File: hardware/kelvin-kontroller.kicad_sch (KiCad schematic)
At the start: 22 parts

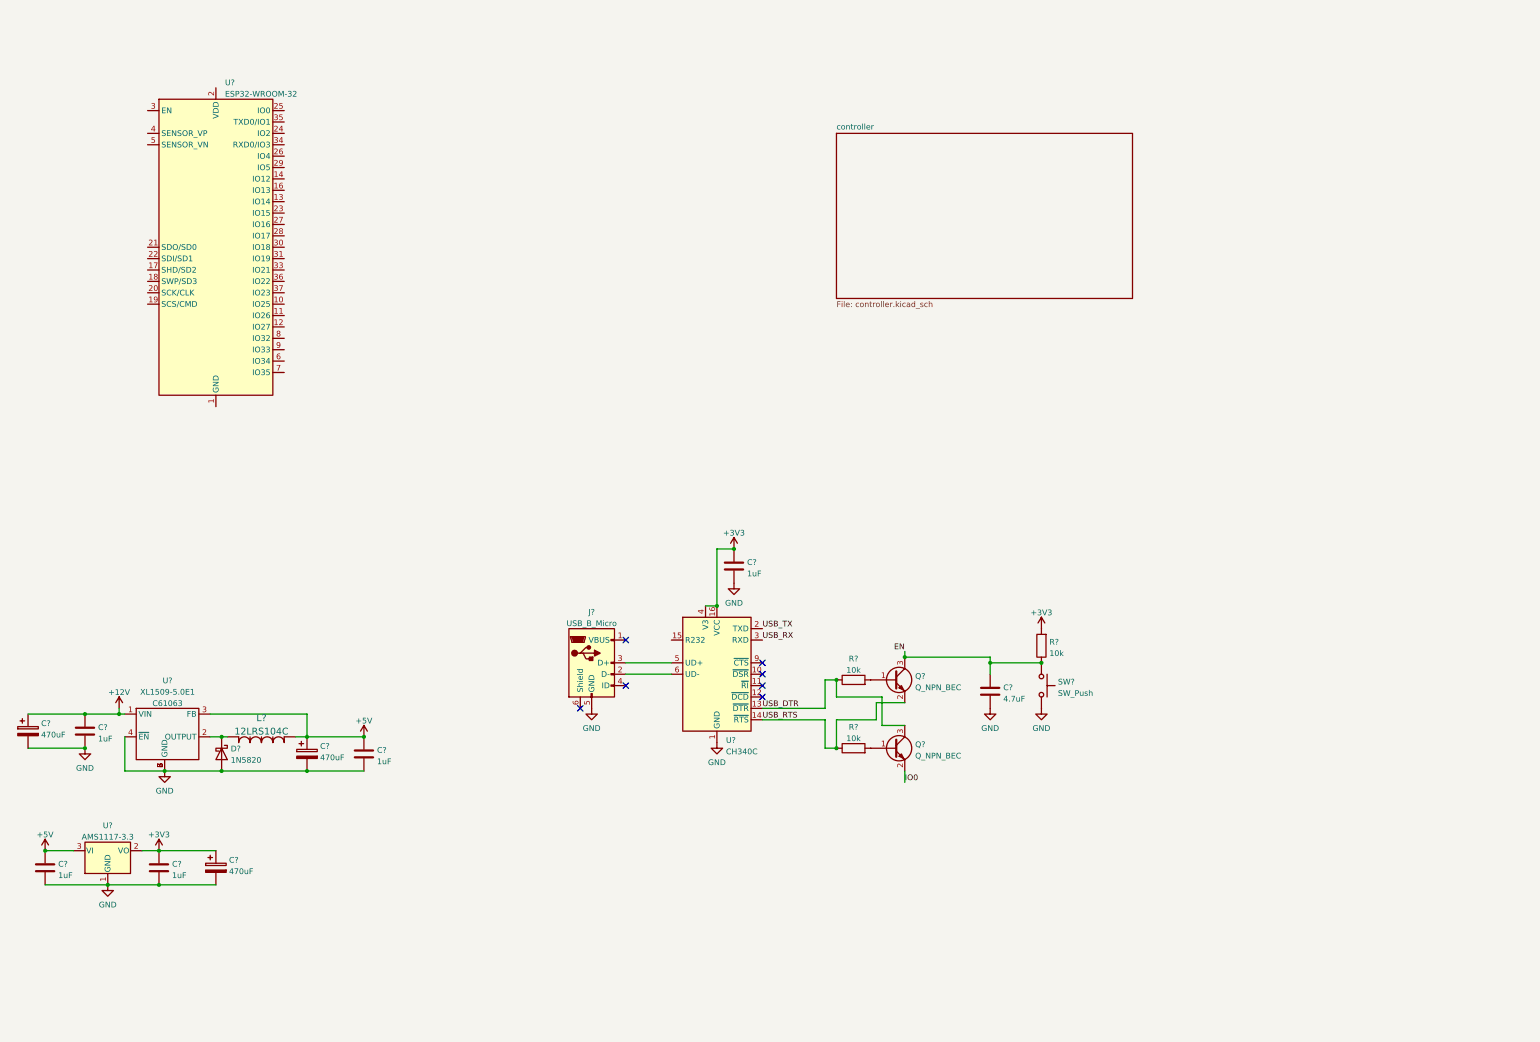
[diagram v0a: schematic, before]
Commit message: Continue schematic - finish controller and add LCD
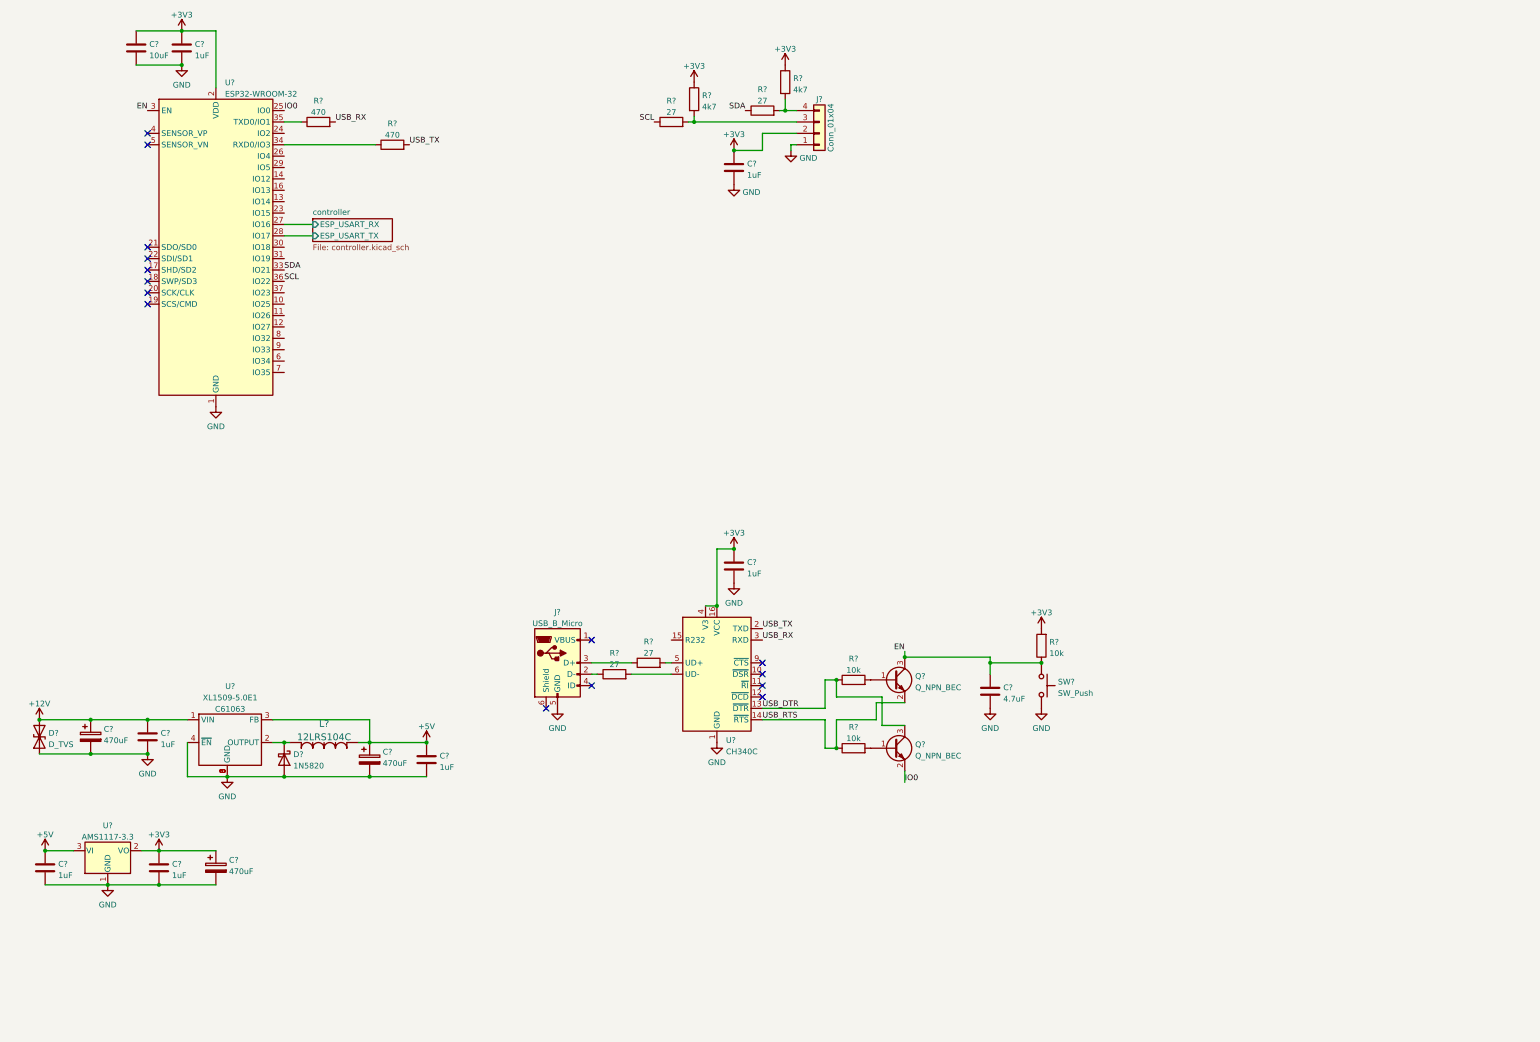
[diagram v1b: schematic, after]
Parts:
- added C? (x2): 1uF, symbol Device:C
- added C?: 10uF, symbol Device:C
- added D?: D_TVS, symbol Device:D_TVS
- added J?: Conn_01x04, symbol Connector_Generic:Conn_01x04
- added R? (x2): 4k7, symbol Device:R
- added R? (x2): 470, symbol Device:R
- added R? (x4): 27, symbol Device:R
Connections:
- net +12V: now also D?.2 (A2)
- net +3V3: now also U?.2 (VDD), C?.1, C?.1, C?.1, J?.2 (Pin_2), R?.1, R?.1
- net EN: now also U?.3 (EN)
- net GND: now also U?.1 (GND), U?.15 (GND), U?.38 (GND), U?.39 (GND), C?.2, C?.2, C?.2, D?.1 (A1), J?.1 (Pin_1)
- net IO0: now also U?.25 (IO0)
- net USB_RX: now also R?.2
- net USB_TX: now also R?.2
- net at J?.2 (D-): now also R?.1; no longer U?.6 (UD-)
- net at J?.3 (D+): now also R?.1; no longer U?.5 (UD+)
- net controller/ESP_USART_RX: now reaches U?.27 (IO16)
- net controller/ESP_USART_TX: now reaches U?.28 (IO17)
- net SDA: now reaches U?.33 (IO21)
- net SDA: now also R?.1
- net at U?.34 (RXD0/IO3): now also R?.1
- net at U?.35 (TXD0/IO1): now also R?.1
- net SCL: now reaches U?.36 (IO22)
- net SCL: now also R?.1
- new net: J?.3 (Pin_3), R?.2, R?.2
- new net: R?.2, U?.5 (UD+)
- new net: R?.2, U?.6 (UD-)
- new net: J?.4 (Pin_4), R?.2, R?.2
- no-connect marks 7 -> 15
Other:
- sheet controller ports: added ESP_USART_RX, ESP_USART_TX; removed none
- moved on the sheet: C?, D?, J?, L?, U?

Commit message: Schematic nearly finished
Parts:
- added C26, C28: 10nF, symbol Device:C
- added C27: 100nF, symbol Device:C
- added J14: Conn_01x02, symbol Connector_Generic:Conn_01x02
- added R31, R32, R33, R35: 10k, symbol Device:R
- added R34: 1k, symbol Device:R
- added SW3: RotaryEncoder_Switch, symbol Device:RotaryEncoder_Switch
- gave numbers to parts that had none: 35
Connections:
- net +12V: now also J14.2 (Pin_2)
- net +3V3: now also R32.1, R33.2
- net GND: now also C26.2, C27.2, C28.2, J14.1 (Pin_1), SW3.C, SW3.S2
- net ENC_BUTTON: now reaches U6.10 (IO25)
- net ENC_BUTTON: now also R34.1
- net ENC_A: now reaches U6.11 (IO26)
- net ENC_A: now also C26.1, R31.2
- net ENC_B: now reaches U6.12 (IO27)
- net ENC_B: now also C28.1, R35.1
- new net: R33.1, R35.2, SW3.A
- new net: R31.1, R32.2, SW3.B
- new net: C27.1, R34.2, SW3.S1
- no-connect marks 15 -> 30
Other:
- note added: "TO SCREEN"

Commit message: Update schematic and part assignment
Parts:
- added C29, C30: 10uF, Capacitor_SMD:C_0603_1608Metric, symbol Device:C
- added J15: Conn_01x07, symbol Connector_Generic:Conn_01x07
- added R36, R39: 100, Resistor_SMD:R_0402_1005Metric, symbol Device:R
- added R37, R38: 1k, Resistor_SMD:R_0402_1005Metric, symbol Device:R
- C14, C17, C18, C19, C22, C23, C24: footprint (none) -> Capacitor_SMD:C_0402_1005Metric; LCSC (none) -> C52923
- C15, C20, C21: MPN (none) -> 25PK1000MEFC10X16
- C16: footprint (none) -> Capacitor_SMD:C_0603_1608Metric; LCSC (none) -> C96446
- C25: footprint (none) -> Capacitor_SMD:C_0402_1005Metric; LCSC (none) -> C23733
- C26, C28: footprint (none) -> Capacitor_SMD:C_0402_1005Metric; LCSC (none) -> C15195
- C27: footprint (none) -> Capacitor_SMD:C_0402_1005Metric; LCSC (none) -> C307331
- D10: value D_TVS -> D_TVS_12V; footprint (none) -> Diode_SMD:D_SMA_Handsoldering; MPN (none) -> 824501131
- D11: footprint Diode_THT:D_DO-201AD_P15.24mm_Horizontal -> Diode_THT:D_DO-201AD_P12.70mm_Horizontal; MPN (none) -> SB10150TA
- J12: LCSC (none) -> C132563
- R20, R21: footprint (none) -> Resistor_SMD:R_0402_1005Metric; LCSC (none) -> C25117
- R22, R23, R24, R26: footprint (none) -> Resistor_SMD:R_0603_1608Metric; LCSC (none) -> C25190
- R25, R27: footprint (none) -> Resistor_SMD:R_0402_1005Metric; LCSC (none) -> C25900
- R28, R29, R30, R31, R32, R33, R35: footprint (none) -> Resistor_SMD:R_0402_1005Metric; LCSC (none) -> C25744
- R34: footprint (none) -> Resistor_SMD:R_0402_1005Metric; LCSC (none) -> C11702
- SW2: footprint (none) -> Homebrew:SW_TACTILE_5.1MM_TS-1187A-C-D-B; LCSC (none) -> C318884
- SW3: footprint (none) -> Homebrew:BOURNS_PEC12R-4xxxF-Sxxxx; MPN (none) -> PEC12R-4230F-S0024
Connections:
- net +3V3: now also C29.1, J15.2 (Pin_2)
- net +5V: now also C30.1, J15.1 (Pin_1)
- net ENC_A: now also U6.9 (IO33); no longer U6.11 (IO26)
- net ENC_B: now also U6.6 (IO34); no longer U6.12 (IO27)
- net ENC_BUTTON: now also U6.8 (IO32); no longer U6.10 (IO25)
- net GND: now also C29.2, C30.2, J15.7 (Pin_7)
- net controller/ESP_USART_RX renamed ESP_USART_RX
- net ESP_USART_RX: now also R39.1
- net controller/ESP_USART_TX renamed ESP_USART_TX
- net ESP_USART_TX: now also R36.1
- new net: J15.6 (Pin_6), R38.2
- new net: J15.5 (Pin_5), R37.2
- new net: J15.3 (Pin_3), R39.2
- new net: J15.4 (Pin_4), R36.2
- new net AUX0: R37.1, U6.11 (IO26)
- new net AUX1: R38.1, U6.12 (IO27)
- no-connect marks 30 -> 28
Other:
- moved on the sheet: C15, C17, C20, C21, C22, D10, D11, L1, U7

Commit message: Finish assigning footprints
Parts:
- J13: value Conn_01x04 -> Conn_01x04 Header Right-angle; footprint (none) -> Connector_PinHeader_2.54mm:PinHeader_1x04_P2.54mm_Horizontal
- J14: value Conn_01x02 -> Conn_01x02 Terminals; footprint (none) -> Homebrew:Amphenol_BarrierStrip_YK321020XX00G_1x02_P7.62; MPN (none) -> YK3210203000G
- J15: value Conn_01x07 -> Conn_01x07 Header; footprint (none) -> Connector_PinHeader_2.54mm:PinHeader_1x07_P2.54mm_Vertical
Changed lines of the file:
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@@
       (effects (font (size 1.27 1.27)) (justify left))
     )
-    (property "Value" "Conn_01x07" (id 1) (at 192.532 93.1422 0)
-      (effects (font (size 1.27 1.27)) (justify left))
-    )
-    (property "Footprint" "" (id 2) (at 190.5 91.44 0)
+    (property "Value" "Conn_01x07 Header" (id 1) (at 192.532 93.1422 0)
+      (effects (font (size 1.27 1.27)) (justify left))
+    )
+    (property "Footprint" "Connector_PinHeader_2.54mm:PinHeader_1x07_P2.54mm_Vertical" (id 2) (at 190.5 91.44 0)
       (effects (font (size 1.27 1.27)) hide)
     )
@@
     (in_bom yes) (on_board yes)
     (property "Reference" "J14" (id 0) (at 22.86 228.6 0))
-    (property "Value" "Conn_01x02" (id 1) (at 20.32 232.41 90))
-    (property "Footprint" "" (id 2) (at 22.86 233.68 0)
+    (property "Value" "Conn_01x02 Terminals" (id 1) (at 20.32 232.41 90))
+    (property "Footprint" "Homebrew:Amphenol_BarrierStrip_YK321020XX00G_1x02_P7.62" (id 2) (at 22.86 233.68 0)
       (effects (font (size 1.27 1.27)) hide)
     )
     (property "Datasheet" "~" (id 3) (at 22.86 233.68 0)
+      (effects (font (size 1.27 1.27)) hide)
+    )
+    (property "MPN" "YK3210203000G" (id 4) (at 22.86 233.68 0)
       (effects (font (size 1.27 1.27)) hide)
     )
@@
     (in_bom yes) (on_board yes)
     (property "Reference" "J13" (id 0) (at 193.04 36.83 0))
-    (property "Value" "Conn_01x04" (id 1) (at 195.58 43.18 90))
-    (property "Footprint" "" (id 2) (at 193.04 44.45 0)
+    (property "Value" "Conn_01x04 Header Right-angle" (id 1) (at 195.58 43.18 90))
+    (property "Footprint" "Connector_PinHeader_2.54mm:PinHeader_1x04_P2.54mm_Horizontal" (id 2) (at 193.04 44.45 0)
       (effects (font (size 1.27 1.27)) hide)
     )
@@
     )
     (path "/e6c26726-7c08-49a7-acb2-990c617cbaaa/5c00dde9-9a25-4b62-bb9a-7808ee1165e4"
-      (reference "J2") (unit 1) (value "Conn_01x04 Header") (footprint "")
+      (reference "J2") (unit 1) (value "Conn_01x04 Header") (footprint "Connector_PinHeader_2.54mm:PinHeader_1x04_P2.54mm_Vertical")
     )
     (path "/e6c26726-7c08-49a7-acb2-990c617cbaaa/6ed19f8c-730b-48e5-baac-0c746f44a0fe"
-      (reference "J3") (unit 1) (value "Conn_01x02") (footprint "")
+      (reference "J3") (unit 1) (value "Conn_01x02 MiniPV") (footprint "Homebrew:MiniPV_76384-X02XX_1x02_P2.54mm_Vertical")
     )
     (path "/e6c26726-7c08-49a7-acb2-990c617cbaaa/c52c0b5e-d508-417c-b245-3c0322c2b175"
-      (reference "J4") (unit 1) (value "Conn_01x02") (footprint "")
-    )
-    (path "/e6c26726-7c08-49a7-acb2-990c617cbaaa/522b46a6-7de9-42fe-b8e0-62921b80488e"
-      (reference "J7") (unit 1) (value "Conn_01x02") (footprint "")
-    )
-    (path "/e6c26726-7c08-49a7-acb2-990c617cbaaa/a597156d-1adc-457e-84a7-f751c1d0549d"
-      (reference "J8") (unit 1) (value "Conn_01x02") (footprint "")
-    )
-    (path "/e6c26726-7c08-49a7-acb2-990c617cbaaa/9e4775dc-175f-4ad1-a42a-8065634c2420"
-      (reference "J9") (unit 1) (value "Conn_01x02") (footprint "")
+      (reference "J4") (unit 1) (value "Conn_01x02 MiniPV") (footprint "Homebrew:MiniPV_76384-X02XX_1x02_P2.54mm_Vertical")
     )
     (path "/e6c26726-7c08-49a7-acb2-990c617cbaaa/34ab0ce4-ca8a-4f83-8b5d-699207168d68"
-      (reference "J10") (unit 1) (value "Conn_01x06 Header") (footprint "")
+      (reference "J10") (unit 1) (value "Conn_01x06 Header") (footprint "Connector_PinHeader_2.54mm:PinHeader_1x06_P2.54mm_Vertical")
     )
     (path "/e6c26726-7c08-49a7-acb2-990c617cbaaa/3f9f4e20-b9db-463d-8dcf-8c61011454d2"
-      (reference "J11") (unit 1) (value "Conn_01x04") (footprint "")
+      (reference "J11") (unit 1) (value "Conn_01x04 MiniPV") (footprint "Connector_PinHeader_2.54mm:PinHeader_1x04_P2.54mm_Vertical")
     )
     (path "/34784a74-0d87-4284-bd23-f47708a5383b"
@@
     )
     (path "/de59f496-7ca2-492a-81b4-2ee0d79a010f"
-      (reference "J13") (unit 1) (value "Conn_01x04") (footprint "")
+      (reference "J13") (unit 1) (value "Conn_01x04 Header Right-angle") (footprint "Connector_PinHeader_2.54mm:PinHeader_1x04_P2.54mm_Horizontal")
     )
     (path "/b2b4c38e-004f-4224-91df-cfc95a83d425"
-      (reference "J14") (unit 1) (value "Conn_01x02") (footprint "")
+      (reference "J14") (unit 1) (value "Conn_01x02 Terminals") (footprint "Homebrew:Amphenol_BarrierStrip_YK321020XX00G_1x02_P7.62")
     )
     (path "/60916c9b-504f-4f1b-b792-32446457f8bc"
-      (reference "J15") (unit 1) (value "Conn_01x07") (footprint "")
-    )
-    (path "/e6c26726-7c08-49a7-acb2-990c617cbaaa/d5f8e761-ba5d-4420-98a1-24146662f7c4"
-      (reference "J16") (unit 1) (value "Conn_01x02 Screw") (footprint "")
+      (reference "J15") (unit 1) (value "Conn_01x07 Header") (footprint "Connector_PinHeader_2.54mm:PinHeader_1x07_P2.54mm_Vertical")
+    )
+    (path "/e6c26726-7c08-49a7-acb2-990c617cbaaa/08b13da6-e960-4584-a5c7-61d970474022"
+      (reference "J?") (unit 1) (value "Conn_01x03 MiniPV") (footprint "Homebrew:MiniPV_69167-X03XXX_1x03_P2.54mm_Polarized_Vertical")
     )
     (path "/e6c26726-7c08-49a7-acb2-990c617cbaaa/18134577-c2d1-40f8-8deb-39a75a43cfd7"
-      (reference "J?") (unit 1) (value "Conn_01x03") (footprint "")
-    )
-    (path "/e6c26726-7c08-49a7-acb2-990c617cbaaa/74fc1024-19b0-4248-8be8-58ee4164edaf"
-      (reference "J?") (unit 1) (value "Conn_01x02") (footprint "")
+      (reference "J?") (unit 1) (value "Conn_01x03 MiniPV") (footprint "Homebrew:MiniPV_69167-X03XXX_1x03_P2.54mm_Polarized_Vertical")
+    )
+    (path "/e6c26726-7c08-49a7-acb2-990c617cbaaa/46853e35-e577-4d7c-93f6-11bdb0020a07"
+      (reference "J?") (unit 1) (value "Conn_01x03 MiniPV") (footprint "Homebrew:MiniPV_69167-X03XXX_1x03_P2.54mm_Polarized_Vertical")
+    )
+    (path "/e6c26726-7c08-49a7-acb2-990c617cbaaa/a2d081cf-e222-4626-8eca-2432d1373a5b"
+      (reference "J?") (unit 1) (value "Conn_01x03 MiniPV") (footprint "Homebrew:MiniPV_69167-X03XXX_1x03_P2.54mm_Polarized_Vertical")
+    )
+    (path "/e6c26726-7c08-49a7-acb2-990c617cbaaa/a4548f62-150b-4139-a191-2f7a2410a17e"
+      (reference "J?") (unit 1) (value "Conn_01x03 MiniPV") (footprint "Homebrew:MiniPV_69167-X03XXX_1x03_P2.54mm_Polarized_Vertical")
     )
     (path "/e6c26726-7c08-49a7-acb2-990c617cbaaa/ba23e2ab-1a26-4b48-984c-0950f4cd565d"
-      (reference "J?") (unit 1) (value "Conn_01x03") (footprint "")
+      (reference "J?") (unit 1) (value "Conn_01x03 MiniPV") (footprint "Homebrew:MiniPV_69167-X03XXX_1x03_P2.54mm_Polarized_Vertical")
+    )
+    (path "/e6c26726-7c08-49a7-acb2-990c617cbaaa/fe76888a-d2dc-456d-99e2-f23ab79140ea"
+      (reference "J?") (unit 1) (value "Conn_01x03 MiniPV") (footprint "Homebrew:MiniPV_69167-X03XXX_1x03_P2.54mm_Polarized_Vertical")
     )
     (path "/e6c26726-7c08-49a7-acb2-990c617cbaaa/065175bc-ea17-46fa-9357-43969de5409f"

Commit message: Start layout
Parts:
- added D14: D, Diode_SMD:D_SMA, symbol Device:D
- added H1, H2, H3, H4: MountingHole, MountingHole:MountingHole_3.2mm_M3, symbol Mechanical:MountingHole
- D11: footprint Diode_THT:D_DO-201AD_P12.70mm_Horizontal -> Diode_SMD:D_SMA; LCSC (none) -> C8678; MPN SB10150TA -> (none)
- J13: value Conn_01x04 Header Right-angle -> Conn_01x04 Header; footprint Connector_PinHeader_2.54mm:PinHeader_1x04_P2.54mm_Horizontal -> Connector_PinHeader_2.54mm:PinHeader_1x04_P2.54mm_Vertical
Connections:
- net +12V: now also D14.1 (K)
- net GND: now also D14.2 (A)
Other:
- note added: "CROWBAR DIODE"
- moved on the sheet: C15, C17, C21, C22, C24, C25, C30, D10, D11, J12, L1, Q5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

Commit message: Add internal thermistor and change SSR2 -> mosfet
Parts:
- removed D14: D, Diode_SMD:D_SMA, symbol Device:D
- removed H1, H2, H3, H4: MountingHole, MountingHole:MountingHole_3.2mm_M3, symbol Mechanical:MountingHole
- D11: footprint Diode_SMD:D_SMA -> Diode_THT:D_DO-201AD_P12.70mm_Horizontal; LCSC C8678 -> (none); MPN (none) -> SB10150TA
- J13: value Conn_01x04 Header -> Conn_01x04 Header Right-angle; footprint Connector_PinHeader_2.54mm:PinHeader_1x04_P2.54mm_Vertical -> Connector_PinHeader_2.54mm:PinHeader_1x04_P2.54mm_Horizontal
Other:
- note removed: "CROWBAR DIODE"
- moved on the sheet: C15, C17, C21, C22, C24, C25, C30, D10, D11, J12, L1, Q5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

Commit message: Continue layout, add SPI flash
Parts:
- added C11: 1uF, Capacitor_SMD:C_0402_1005Metric, symbol Device:C
- added D14: D, Diode_SMD:D_SMA, symbol Device:D
- added H1, H2, H3, H4: MountingHole, MountingHole:MountingHole_3.2mm_M3, symbol Mechanical:MountingHole
- added U9: W25Q128JVSIQ, Package_SO:SOIC-8_5.275x5.275mm_P1.27mm, symbol Homebrew:W25Q128JVSIQ
- D11: footprint Diode_THT:D_DO-201AD_P12.70mm_Horizontal -> Diode_SMD:D_SMA; LCSC (none) -> C8678; MPN SB10150TA -> (none)
- J13: value Conn_01x04 Header Right-angle -> Conn_01x04 Header; footprint Connector_PinHeader_2.54mm:PinHeader_1x04_P2.54mm_Horizontal -> Connector_PinHeader_2.54mm:PinHeader_1x04_P2.54mm_Vertical
- R22, R23, R24, R26: value 27 -> 22; footprint Resistor_SMD:R_0603_1608Metric -> Resistor_SMD:R_0402_1005Metric; LCSC C25190 -> C25091
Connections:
- net +12V: now also D14.1 (K)
- net +3V3: now also C11.1, U9.8 (VCC)
- net GND: now also C11.2, D14.2 (A), U9.4 (GND)
- net SCL: now also U6.26 (IO4); no longer U6.36 (IO22)
- net SDA: now also U6.16 (IO13); no longer U6.33 (IO21)
- net USB-: now reaches J12.2 (D-), R22.1
- net USB+: now reaches J12.3 (D+), R23.1
- net VSPI_CS: now reaches U6.29 (IO5)
- net VSPI_CS: now also U9.1 (/CS)
- net VSPI_SCK: now reaches U6.30 (IO18)
- net VSPI_SCK: now also U9.6 (CLK)
- net VSPI_MISO: now reaches U6.31 (IO19)
- net VSPI_MISO: now also U9.2 (DO(IO1))
- net VSPI_MOSI: now reaches U6.37 (IO23)
- net VSPI_MOSI: now also U9.5 (DI(IO0))
- net USB_R+: now reaches R23.2, U8.5 (UD+)
- net USB_R-: now reaches R22.2, U8.6 (UD-)
- new net VSPI_HD: U6.33 (IO21), U9.7 (/HOLD/RESET(IO3))
- new net VSPI_WP: U6.36 (IO22), U9.3 (/WP(IO2))
- no-connect marks 28 -> 22
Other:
- note added: "CROWBAR DIODE"
- moved on the sheet: C15, C17, C21, C22, C24, C25, C30, D10, D11, J12, L1, Q5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
